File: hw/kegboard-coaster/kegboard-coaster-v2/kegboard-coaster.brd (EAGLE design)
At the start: 38.1 x 17.8 mm, 8 parts

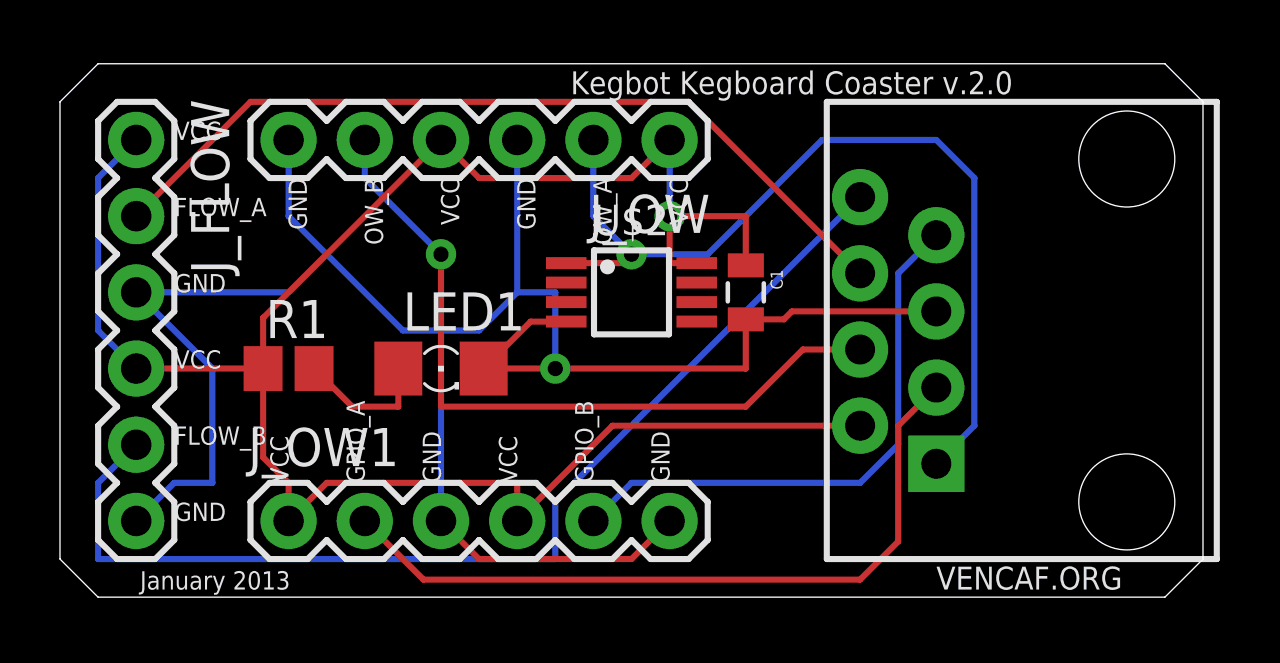
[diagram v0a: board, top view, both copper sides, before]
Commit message: Fix temp. sensor REFDES
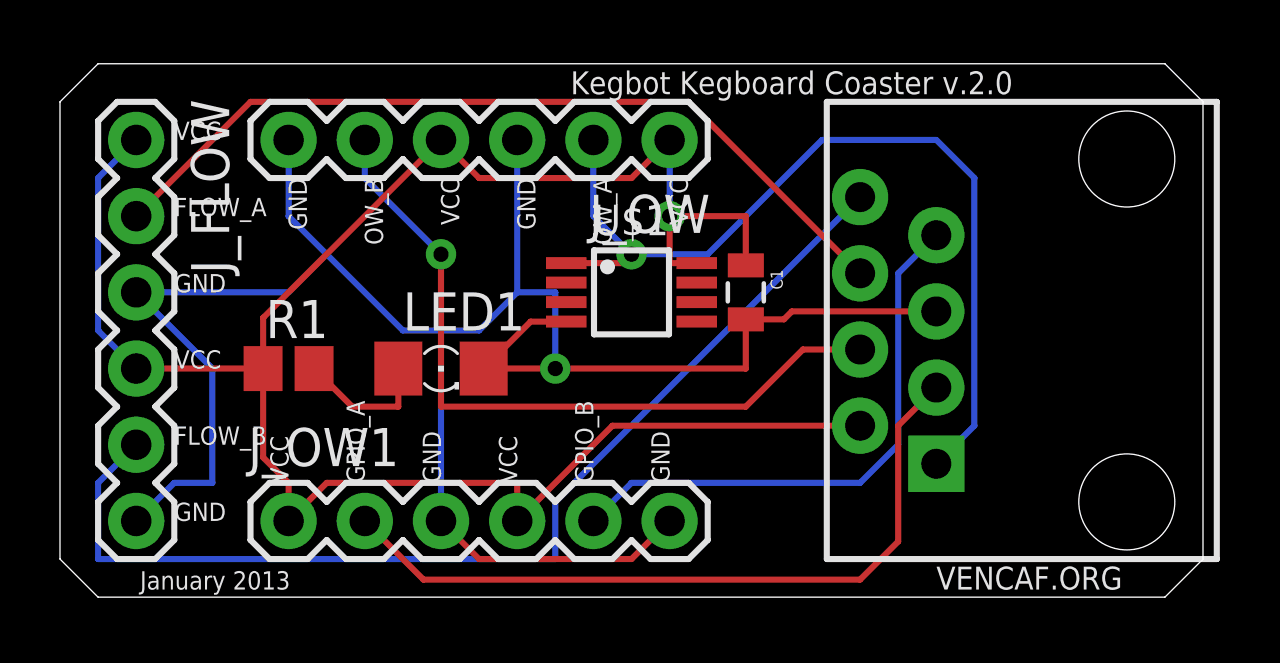
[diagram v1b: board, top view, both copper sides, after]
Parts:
- renumbered U$2 to U$1
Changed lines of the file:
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@@
 <element name="LED1" library="SparkFun-LED" package="FKIT-LED-1206" value="" x="12.7" y="7.62"/>
 <element name="C1" library="SparkFun-Passives" package="0805" value="0.1 uF" x="22.86" y="10.16" rot="R270"/>
-<element name="U$2" library="geoffculp" package="UMAX8" value="TEMPERATURE-SENSORUMAX8" x="19.05" y="10.16" rot="R270"/>
+<element name="U$1" library="geoffculp" package="UMAX8" value="TEMPERATURE-SENSORUMAX8" x="19.05" y="10.16" rot="R270"/>
 </elements>
 <signals>
@@
 <contactref element="HEADER-RJ1" pad="1"/>
 <contactref element="J_OW" pad="2"/>
-<contactref element="U$2" pad="1"/>
+<contactref element="U$1" pad="1"/>
 <wire x1="19.05" y1="11.43" x2="21.59" y2="11.43" width="0.2032" layer="16"/>
 <wire x1="21.59" y1="11.43" x2="25.4" y2="15.24" width="0.2032" layer="16"/>
@@
 <contactref element="R1" pad="1"/>
 <contactref element="C1" pad="1"/>
-<contactref element="U$2" pad="8"/>
+<contactref element="U$1" pad="8"/>
 <wire x1="15.24" y1="2.54" x2="18.415" y2="5.715" width="0.2032" layer="1"/>
 <wire x1="18.415" y1="5.715" x2="26.67" y2="5.715" width="0.2032" layer="1"/>
@@
 <contactref element="LED1" pad="C"/>
 <contactref element="C1" pad="2"/>
-<contactref element="U$2" pad="4"/>
+<contactref element="U$1" pad="4"/>
 <wire x1="13.97" y1="8.89" x2="15.24" y2="10.16" width="0.2032" layer="16"/>
 <wire x1="16.51" y1="10.16" x2="15.24" y2="10.16" width="0.2032" layer="16"/>

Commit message: Fix trace between resistor & LED
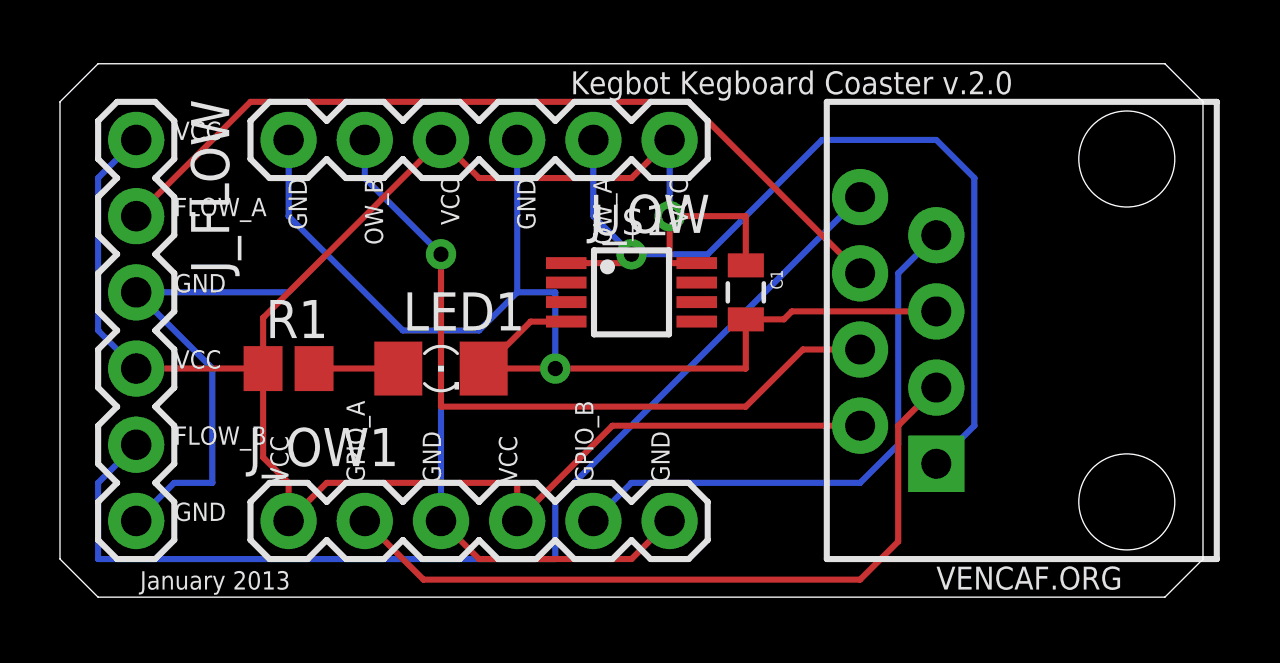
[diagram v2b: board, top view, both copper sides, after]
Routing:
- net N$1: track 4.60 -> 2.81 mm
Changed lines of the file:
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@@
 <contactref element="LED1" pad="A"/>
 <contactref element="R1" pad="2"/>
-<wire x1="8.4700125" y1="7.62" x2="9.7400125" y2="6.35" width="0.2032" layer="1"/>
-<wire x1="9.7400125" y1="6.35" x2="11.27800625" y2="6.35" width="0.2032" layer="1"/>
-<wire x1="11.27800625" y1="6.35" x2="11.27800625" y2="7.62" width="0.2032" layer="1"/>
-<wire x1="11.27800625" y1="7.62" x2="11.278" y2="7.62" width="0" layer="19" extent="1-1"/>
-<wire x1="8.47" y1="7.62" x2="8.4700125" y2="7.62" width="0" layer="19" extent="1-1"/>
+<wire x1="8.47" y1="7.62" x2="11.278" y2="7.62" width="0.2032" layer="1"/>
 </signal>
 </signals>
